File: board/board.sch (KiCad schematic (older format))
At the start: 23 parts, among them CON1 NRF24L01+MODULE, CON2 AVR-ISP-6, CON3 DEBUG, IC1 ATMEGA88PA-A, SW1 SW_PUSH, U1 XR1151

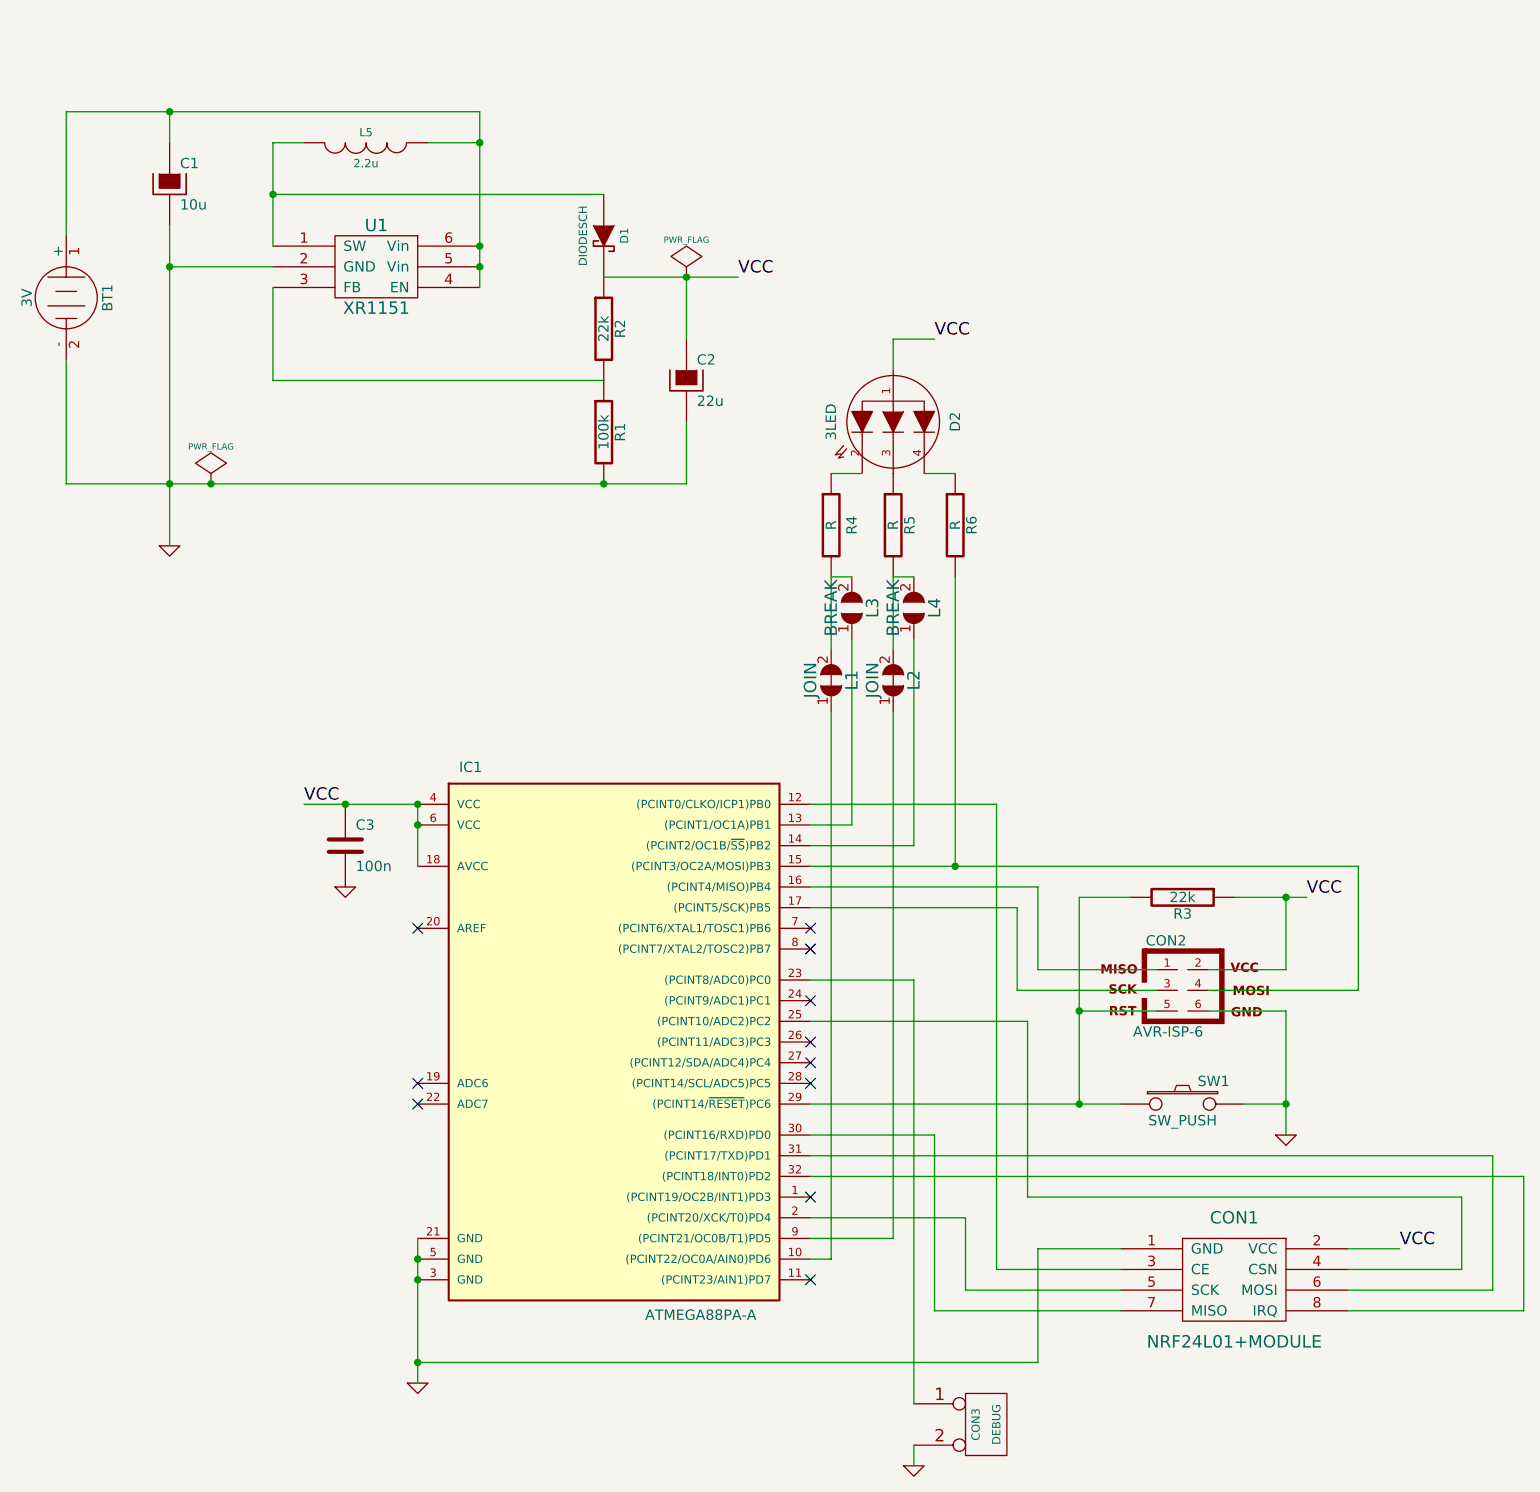
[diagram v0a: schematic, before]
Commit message: - Added MCU control of the "enable" line  - Corrected the XR1151 voltage adjustment resistors (maybe)
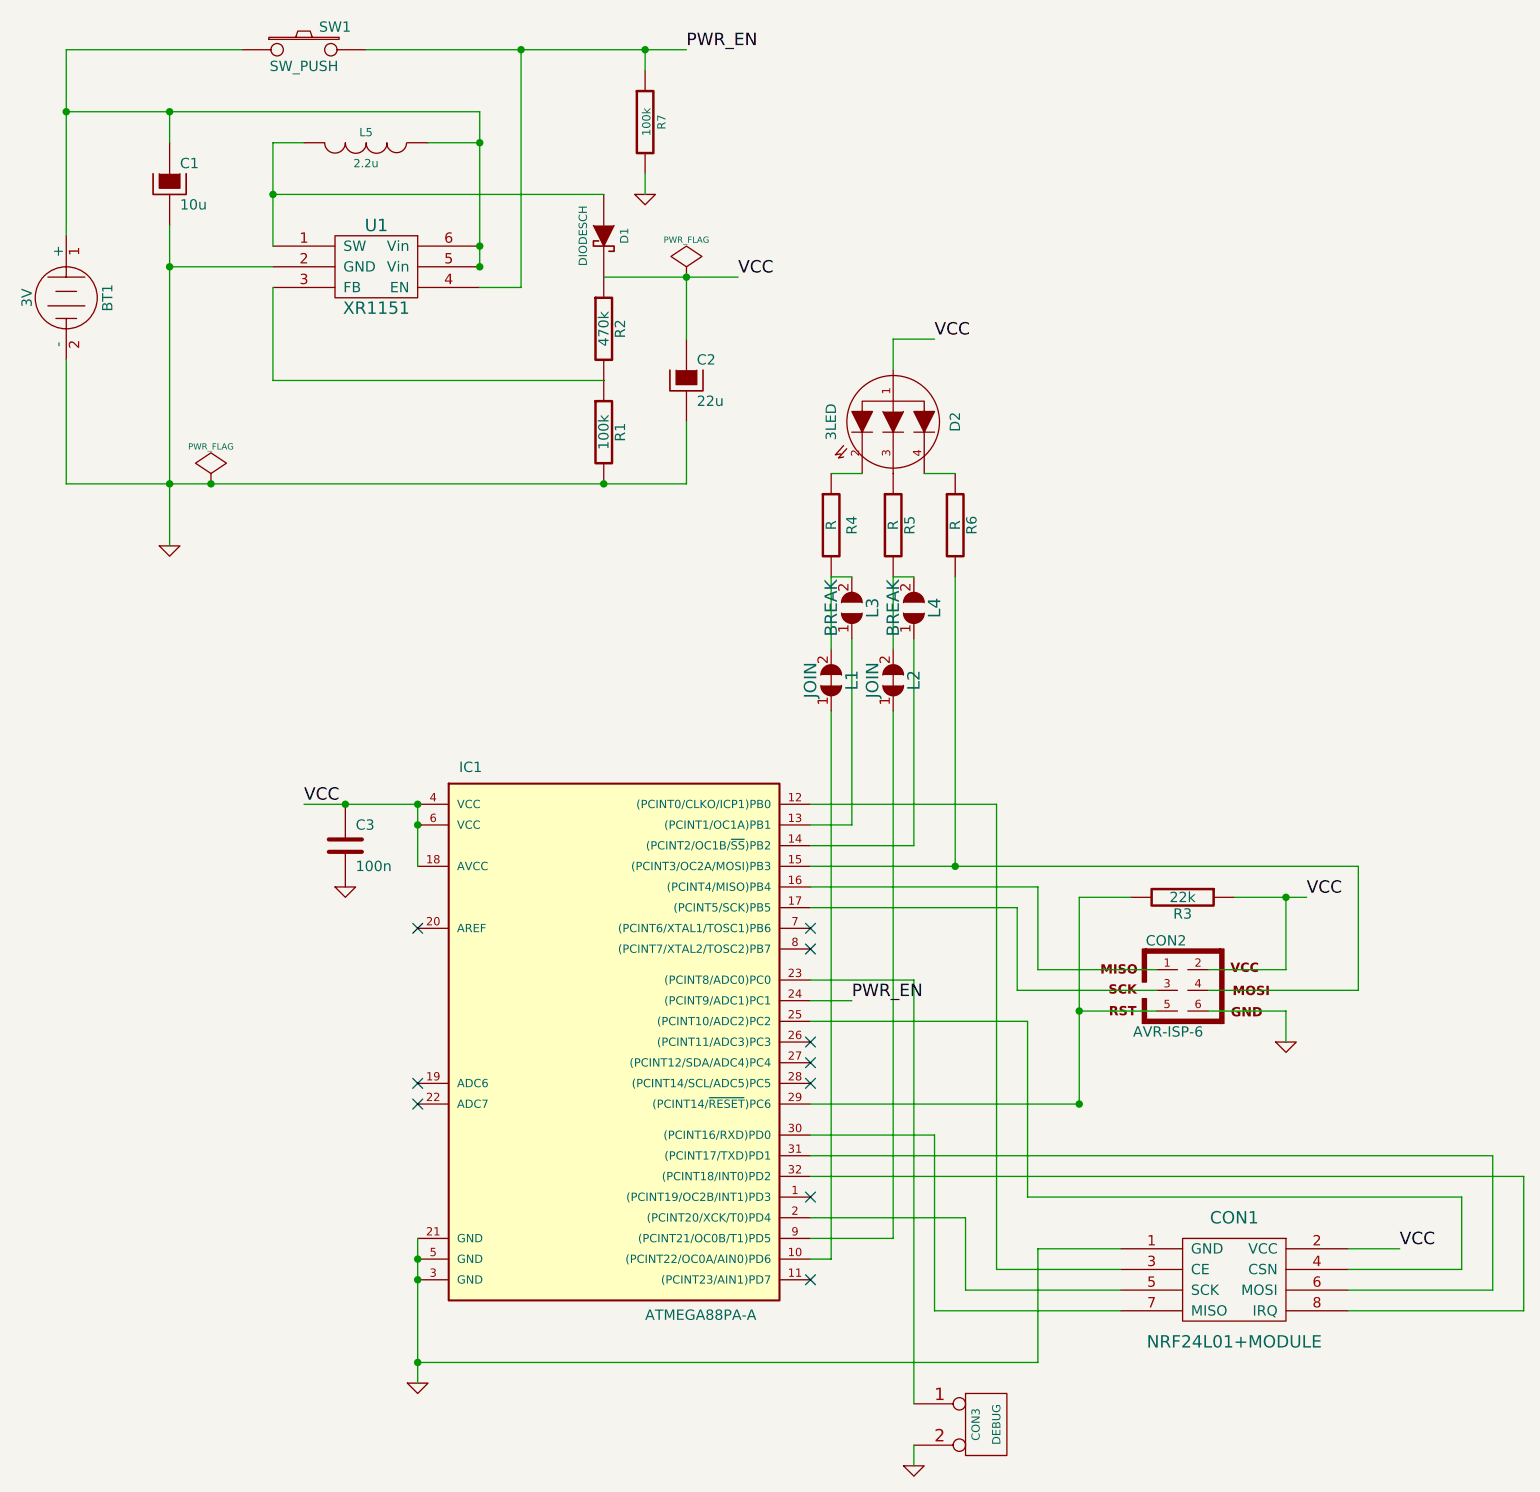
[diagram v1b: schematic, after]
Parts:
- added R7: 100k, ~, symbol R
- R2: value 22k -> 470k
- SW1: footprint (none) -> ~
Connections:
- net GND: now also R7.2; no longer SW1.2
- net PWR_EN: now reaches IC1.24 ((PCINT9/ADC1)PC1)
- net PWR_EN: now also SW1.2, U1.4 (EN), R7.1
- net at CON2.5, IC1.29 ((PCINT14/~RESET~)PC6), R3.2: no longer SW1.1
- net at BT1.1 (+), C1.1, L5.1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: now also SW1.1; no longer U1.4 (EN)
- no-connect marks 11 -> 10
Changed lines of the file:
@@
-EESchema Schematic File Version 2  date Thu 27 Mar 2014 20:42:43 CST
+EESchema Schematic File Version 2
 LIBS:power
 LIBS:device
@@
 LIBS:pads
 LIBS:board-cache
-EELAYER 25  0
+EELAYER 27 0
 EELAYER END
-$Descr A4 11700 8267
+$Descr A4 11693 8268
 encoding utf-8
 Sheet 1 1
 Title ""
-Date "27 mar 2014"
+Date "18 may 2014"
 Rev ""
 Comp ""
@@
 NoConn ~ 4600 5700
 NoConn ~ 4600 5600
-NoConn ~ 4600 5400
 NoConn ~ 4600 5150
 NoConn ~ 4600 5050
@@
 F 0 "#FLG01" H 1700 2995 30  0001 C CNN
 F 1 "PWR_FLAG" H 1700 3080 30  0000 C CNN
+F 2 "" H 1700 2900 60  0001 C CNN
+F 3 "" H 1700 2900 60  0001 C CNN
 	1    1700 2900
 	1    0    0    -1
@@
 F 0 "#FLG02" H 4000 1995 30  0001 C CNN
 F 1 "PWR_FLAG" H 4000 2080 30  0000 C CNN
+F 2 "" H 4000 1900 60  0001 C CNN
+F 3 "" H 4000 1900 60  0001 C CNN
 	1    4000 1900
 	1    0    0    -1
@@
 Connection ~ 5900 5900
 Wire Wire Line
-	4600 5900 6100 5900
-Wire Wire Line
 	6525 5350 7250 5350
 Wire Wire Line
 	7250 5350 7250 4750
 Wire Wire Line
-	6900 6050 6900 5450
-Wire Wire Line
-	6900 5450 6525 5450
-Wire Wire Line
-	5900 5900 5900 4900
+	6525 5450 6900 5450
+Wire Wire Line
+	5900 4900 5900 5900
 Wire Wire Line
 	6900 4900 6900 5250
@@
 	1500 1250 1500 1100
 Wire Wire Line
-	2000 1750 2000 1250
+	2000 1250 2000 1750
 Wire Wire Line
 	2000 1250 2150 1250
@@
 	2150 4450 2700 4450
 Wire Wire Line
-	4250 1900 3600 1900
+	3600 1900 4250 1900
 Connection ~ 4000 1900
 Connection ~ 2700 6750
@@
 Connection ~ 6900 4900
 Wire Wire Line
-	6700 5900 6900 5900
-Connection ~ 6900 5900
-Wire Wire Line
-	1000 1100 1000 1700
+	1000 800  1000 1700
 Connection ~ 1500 1100
-Wire Wire Line
-	3000 1100 3000 1950
 Wire Wire Line
 	2700 4450 2700 4750
@@
 F 0 "#PWR03" H 5100 7650 30  0001 C CNN
 F 1 "GND" H 5100 7580 30  0001 C CNN
+F 2 "" H 5100 7650 60  0001 C CNN
+F 3 "" H 5100 7650 60  0001 C CNN
 	1    5100 7650
 	1    0    0    -1
@@
 F 0 "CON3" V 5400 7450 40  0000 C CNN
 F 1 "DEBUG" V 5500 7450 40  0000 C CNN
+F 2 "" H 5450 7450 60  0001 C CNN
+F 3 "" H 5450 7450 60  0001 C CNN
 	1    5450 7450
 	1    0    0    -1
@@
 F 0 "L2" H 5000 3750 60  0000 C CNN
 F 1 "JOIN" H 5000 3950 60  0000 C CNN
+F 2 "" H 5000 3850 60  0001 C CNN
+F 3 "" H 5000 3850 60  0001 C CNN
 	1    5000 3850
 	0    -1   -1   0
@@
 F 0 "L1" H 4700 3750 60  0000 C CNN
 F 1 "JOIN" H 4700 3950 60  0000 C CNN
+F 2 "" H 4700 3850 60  0001 C CNN
+F 3 "" H 4700 3850 60  0001 C CNN
 	1    4700 3850
 	0    -1   -1   0
@@
 F 0 "L4" H 5100 3400 60  0000 C CNN
 F 1 "BREAK" H 5100 3600 60  0000 C CNN
+F 2 "" H 5100 3500 60  0001 C CNN
+F 3 "" H 5100 3500 60  0001 C CNN
 	1    5100 3500
 	0    -1   -1   0
@@
 F 0 "L3" H 4800 3400 60  0000 C CNN
 F 1 "BREAK" H 4800 3600 60  0000 C CNN
+F 2 "" H 4800 3500 60  0001 C CNN
+F 3 "" H 4800 3500 60  0001 C CNN
 	1    4800 3500
 	0    -1   -1   0
@@
 F 0 "D2" H 5000 2900 50  0000 C CNN
 F 1 "3LED" H 5000 2300 50  0000 C CNN
+F 2 "" H 5000 2600 60  0001 C CNN
+F 3 "" H 5000 2600 60  0001 C CNN
 	1    5000 2600
 	0    1    1    0
@@
 F 0 "BT1" H 1000 2200 50  0000 C CNN
 F 1 "3V" H 1000 1810 50  0000 C CNN
+F 2 "" H 1000 2000 60  0001 C CNN
+F 3 "" H 1000 2000 60  0001 C CNN
 	1    1000 2000
 	0    1    1    0
@@
 F 0 "#PWR04" H 2350 4850 30  0001 C CNN
 F 1 "GND" H 2350 4780 30  0001 C CNN
+F 2 "" H 2350 4850 60  0001 C CNN
+F 3 "" H 2350 4850 60  0001 C CNN
 	1    2350 4850
 	1    0    0    -1
@@
 F 0 "C3" H 2400 4750 50  0000 L CNN
 F 1 "100n" H 2400 4550 50  0000 L CNN
+F 2 "" H 2350 4650 60  0001 C CNN
+F 3 "" H 2350 4650 60  0001 C CNN
 	1    2350 4650
-	1    0    0    -1
-$EndComp
-$Comp
-L SW_PUSH SW1
-U 1 1 532E9D9B
-P 6400 5900
-F 0 "SW1" H 6550 6010 50  0000 C CNN
-F 1 "SW_PUSH" H 6400 5820 50  0000 C CNN
-	1    6400 5900
 	1    0    0    -1
 $EndComp
@@
 F 0 "R3" V 6480 4900 50  0000 C CNN
 F 1 "22k" V 6400 4900 50  0000 C CNN
+F 2 "" H 6400 4900 60  0001 C CNN
+F 3 "" H 6400 4900 60  0001 C CNN
 	1    6400 4900
 	0    1    1    0
@@
 L GND #PWR05
 U 1 1 532E9CA2
-P 6900 6050
-F 0 "#PWR05" H 6900 6050 30  0001 C CNN
-F 1 "GND" H 6900 5980 30  0001 C CNN
-	1    6900 6050
+P 6900 5600
+F 0 "#PWR05" H 6900 5600 30  0001 C CNN
+F 1 "GND" H 6900 5530 30  0001 C CNN
+F 2 "" H 6900 5600 60  0001 C CNN
+F 3 "" H 6900 5600 60  0001 C CNN
+	1    6900 5600
 	1    0    0    -1
 $EndComp
@@
 F 1 "AVR-ISP-6" H 6160 5120 50  0000 L BNN
 F 2 "AVR-ISP-6" V 5880 5390 50  0001 C CNN
+F 3 "" H 6400 5350 60  0001 C CNN
 	1    6400 5350
 	1    0    0    -1
@@
 F 0 "R6" V 5380 3100 50  0000 C CNN
 F 1 "R" V 5300 3100 50  0000 C CNN
+F 2 "" H 5300 3100 60  0001 C CNN
+F 3 "" H 5300 3100 60  0001 C CNN
 	1    5300 3100
 	1    0    0    -1
@@
 F 0 "R5" V 5080 3100 50  0000 C CNN
 F 1 "R" V 5000 3100 50  0000 C CNN
+F 2 "" H 5000 3100 60  0001 C CNN
+F 3 "" H 5000 3100 60  0001 C CNN
 	1    5000 3100
 	1    0    0    -1
@@
 F 0 "R4" V 4800 3100 50  0000 C CNN
 F 1 "R" V 4700 3100 50  0000 C CNN
+F 2 "" H 4700 3100 60  0001 C CNN
+F 3 "" H 4700 3100 60  0001 C CNN
 	1    4700 3100
 	1    0    0    -1
@@
 F 0 "#PWR06" H 2700 7250 30  0001 C CNN
 F 1 "GND" H 2700 7180 30  0001 C CNN
+F 2 "" H 2700 7250 60  0001 C CNN
+F 3 "" H 2700 7250 60  0001 C CNN
 	1    2700 7250
 	1    0    0    -1
@@
 F 0 "C2" H 4050 2500 50  0000 L CNN
 F 1 "22u" H 4050 2300 50  0000 L CNN
+F 2 "" H 4000 2400 60  0001 C CNN
+F 3 "" H 4000 2400 60  0001 C CNN
 	1    4000 2400
 	1    0    0    -1
@@
 F 0 "C1" H 1550 1550 50  0000 L CNN
 F 1 "10u" H 1550 1350 50  0000 L CNN
+F 2 "" H 1500 1450 60  0001 C CNN
+F 3 "" H 1500 1450 60  0001 C CNN
 	1    1500 1450
 	1    0    0    -1
@@
 F 0 "D1" H 3600 1800 40  0000 C CNN
 F 1 "DIODESCH" H 3600 1600 40  0000 C CNN
+F 2 "" H 3600 1700 60  0001 C CNN
+F 3 "" H 3600 1700 60  0001 C CNN
 	1    3600 1700
 	0    1    1    0
@@
 F 0 "L5" V 2400 1250 40  0000 C CNN
 F 1 "2.2u" V 2550 1250 40  0000 C CNN
+F 2 "" H 2450 1250 60  0001 C CNN
+F 3 "" H 2450 1250 60  0001 C CNN
 	1    2450 1250
 	0    1    1    0
@@
 F 0 "#PWR07" H 1500 3200 30  0001 C CNN
 F 1 "GND" H 1500 3130 30  0001 C CNN
+F 2 "" H 1500 3200 60  0001 C CNN
+F 3 "" H 1500 3200 60  0001 C CNN
 	1    1500 3200
 	1    0    0    -1
@@
 F 0 "R1" V 3680 2650 50  0000 C CNN
 F 1 "100k" V 3600 2650 50  0000 C CNN
+F 2 "" H 3600 2650 60  0001 C CNN
+F 3 "" H 3600 2650 60  0001 C CNN
 	1    3600 2650
 	1    0    0    -1
@@
 P 3600 2150
 F 0 "R2" V 3680 2150 50  0000 C CNN
-F 1 "22k" V 3600 2150 50  0000 C CNN
+F 1 "470k" V 3600 2150 50  0000 C CNN
+F 2 "" H 3600 2150 60  0001 C CNN
+F 3 "" H 3600 2150 60  0001 C CNN
 	1    3600 2150
 	1    0    0    -1
@@
 F 0 "U1" H 2500 2050 60  0000 C CNN
 F 1 "XR1151" H 2500 1650 60  0000 C CNN
+F 2 "" H 2500 1850 60  0001 C CNN
+F 3 "" H 2500 1850 60  0001 C CNN
 	1    2500 1850
 	1    0    0    -1
@@
 F 1 "ATMEGA88PA-A" H 3800 4150 50  0000 L BNN
 F 2 "TQFP32" H 3050 4200 50  0001 C CNN
+F 3 "" H 3600 5550 60  0001 C CNN
 	1    3600 5550
 	1    0    0    -1
@@
 F 0 "CON1" H 6650 7050 60  0000 C CNN
 F 1 "NRF24L01+MODULE" H 6650 6450 60  0000 C CNN
+F 2 "" H 6650 6750 60  0001 C CNN
+F 3 "" H 6650 6750 60  0001 C CNN
 	1    6650 6750
 	1    0    0    -1
 $EndComp
+Text Label 4800 5400 0    60   ~ 0
+PWR_EN
+Wire Wire Line
+	4800 5400 4600 5400
+Wire Wire Line
+	3000 1100 3000 1850
+$Comp
+L SW_PUSH SW1
+U 1 1 537805C1
+P 2150 800
+F 0 "SW1" H 2300 910 50  0000 C CNN
+F 1 "SW_PUSH" H 2150 720 50  0000 C CNN
+F 2 "~" H 2150 800 60  0000 C CNN
+F 3 "~" H 2150 800 60  0000 C CNN
+	1    2150 800
+	1    0    0    -1
+$EndComp
+Connection ~ 1000 1100
+Wire Wire Line
+	2450 800  4000 800
+Text Label 4000 800  0    60   ~ 0
+PWR_EN
+Wire Wire Line
+	1000 800  1850 800
+Wire Wire Line
+	3200 800  3200 1950
+Wire Wire Line
+	3200 1950 3000 1950
+Connection ~ 3200 800
+Wire Wire Line
+	5900 5900 4600 5900
+Wire Wire Line
+	6900 5450 6900 5600
+$Comp
+L R R7
+U 1 1 53780B19
+P 3800 1150
+F 0 "R7" V 3880 1150 40  0000 C CNN
+F 1 "100k" V 3807 1151 40  0000 C CNN
+F 2 "~" V 3730 1150 30  0000 C CNN
+F 3 "~" H 3800 1150 30  0000 C CNN
+	1    3800 1150
+	1    0    0    -1
+$EndComp
+Wire Wire Line
+	3800 800  3800 900
+Connection ~ 3800 800
+$Comp
+L GND #PWR?
+U 1 1 53780C06
+P 3800 1500
+F 0 "#PWR?" H 3800 1500 30  0001 C CNN
+F 1 "GND" H 3800 1430 30  0001 C CNN
+F 2 "" H 3800 1500 60  0000 C CNN
+F 3 "" H 3800 1500 60  0000 C CNN
+	1    3800 1500
+	1    0    0    -1
+$EndComp
+Wire Wire Line
+	3800 1400 3800 1500
 $EndSCHEMATC
